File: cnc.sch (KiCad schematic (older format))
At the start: 9 parts, among them CON101 SD_Card, U101 pic32

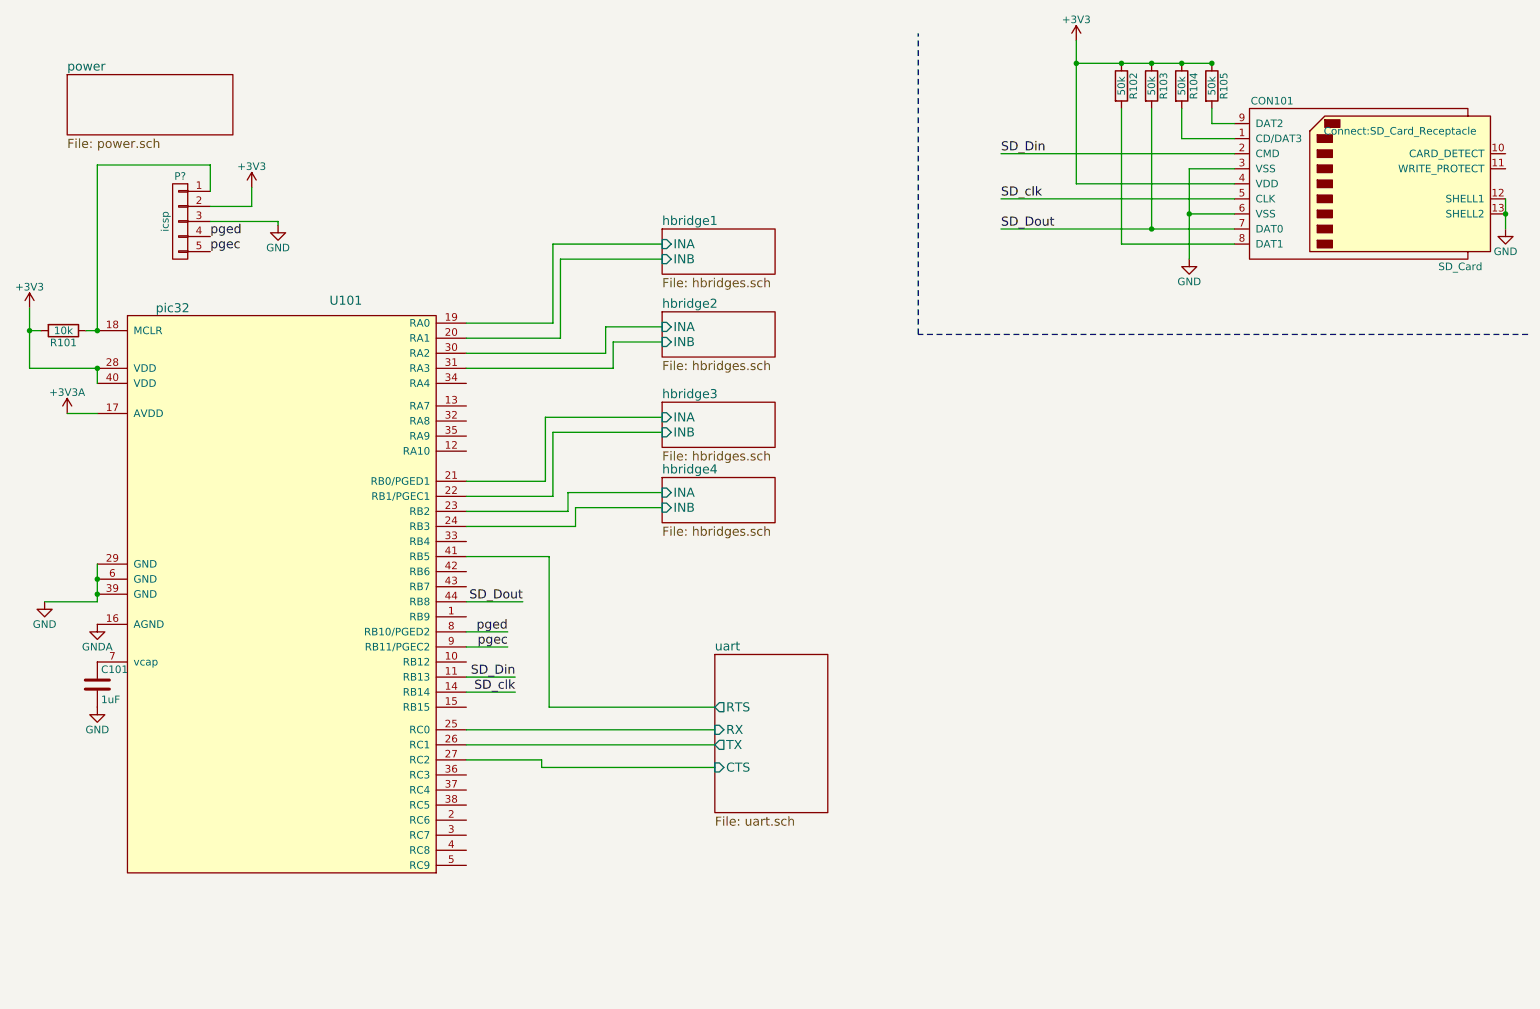
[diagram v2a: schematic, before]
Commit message: Routed a h-bridge. Damn that's a lot of work.
also assigned a lot of components.
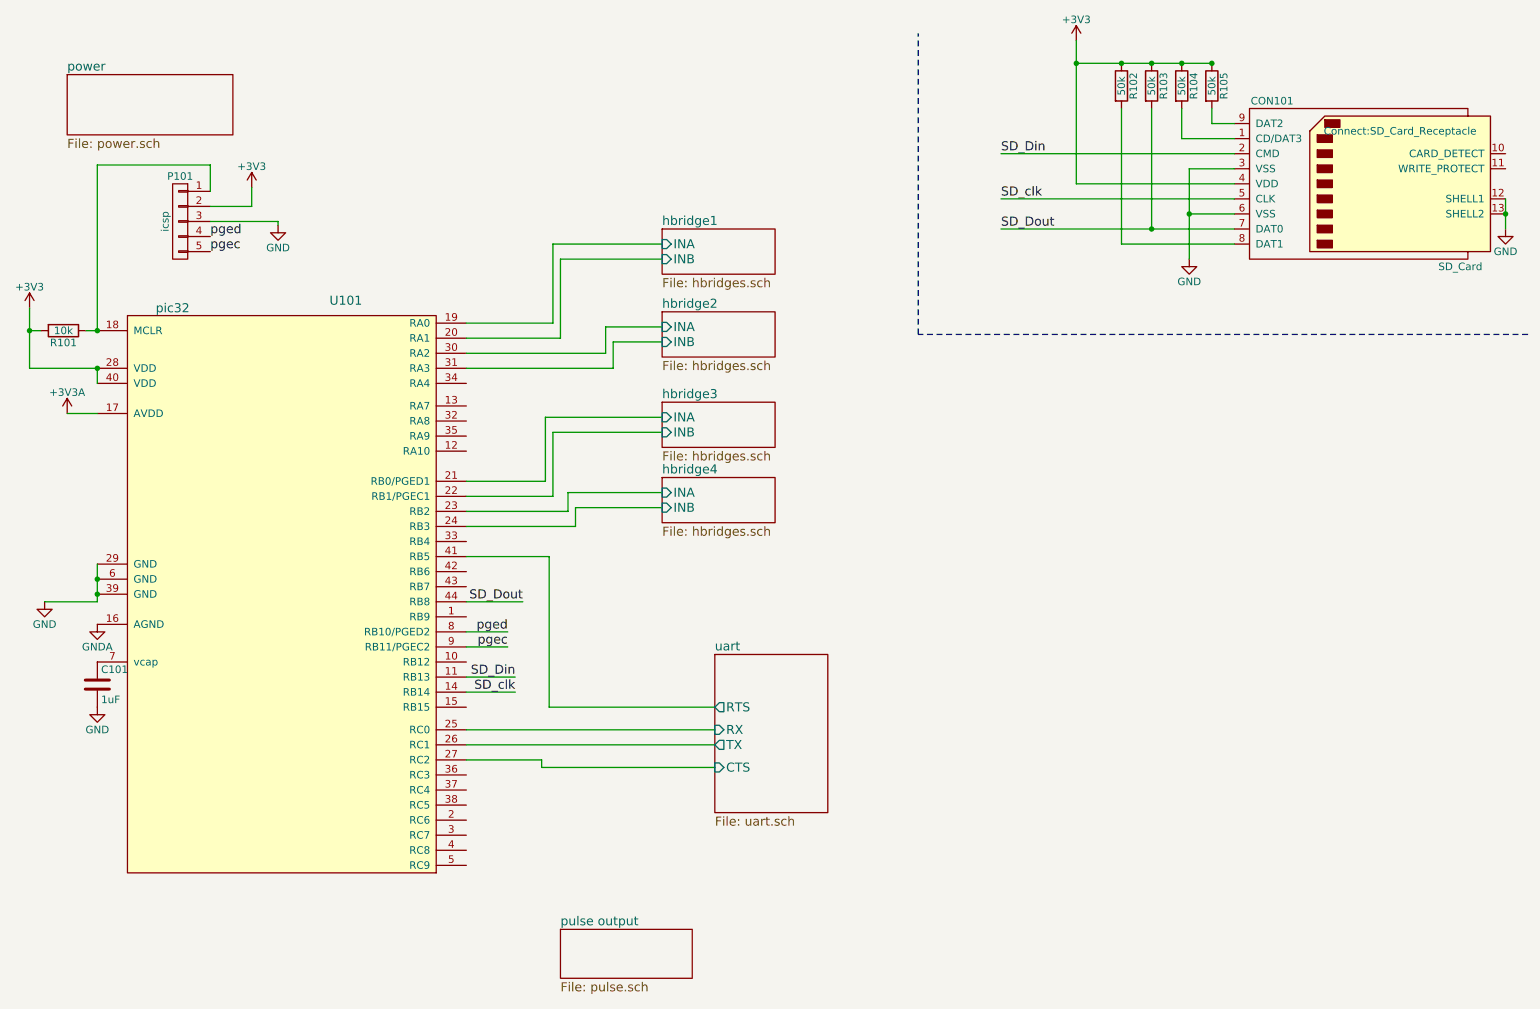
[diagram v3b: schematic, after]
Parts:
- P101: renamed from P?; footprint (none) -> Pin_Headers:Pin_Header_Straight_1x05
- R101, R102, R103, R104, R105: footprint Resistors_SMD:R_0805_HandSoldering -> lib:R_0402_handsoldering
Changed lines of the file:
@@
 $Descr A4 11693 8268
 encoding utf-8
-Sheet 1 7
+Sheet 1 8
 Title ""
 Date ""
@@
 F 0 "R101" V 1405 2675 50  0000 C CNN
 F 1 "10k" V 1325 2675 50  0000 C CNN
-F 2 "Resistors_SMD:R_0805_HandSoldering" V 1255 2675 50  0001 C CNN
+F 2 "lib:R_0402_handsoldering" V 1255 2675 50  0001 C CNN
 F 3 "" H 1325 2675 50  0000 C CNN
 	1    1325 2675
@@
 F 0 "R105" V 9030 1050 50  0000 C CNN
 F 1 "50k" V 8950 1050 50  0000 C CNN
-F 2 "Resistors_SMD:R_0805_HandSoldering" V 8880 1050 50  0001 C CNN
+F 2 "lib:R_0402_handsoldering" V 8880 1050 50  0001 C CNN
 F 3 "" H 8950 1050 50  0000 C CNN
 	1    8950 1050
@@
 F 0 "R104" V 8830 1050 50  0000 C CNN
 F 1 "50k" V 8750 1050 50  0000 C CNN
-F 2 "Resistors_SMD:R_0805_HandSoldering" V 8680 1050 50  0001 C CNN
+F 2 "lib:R_0402_handsoldering" V 8680 1050 50  0001 C CNN
 F 3 "" H 8750 1050 50  0000 C CNN
 	1    8750 1050
@@
 F 0 "R103" V 8630 1050 50  0000 C CNN
 F 1 "50k" V 8550 1050 50  0000 C CNN
-F 2 "Resistors_SMD:R_0805_HandSoldering" V 8480 1050 50  0001 C CNN
+F 2 "lib:R_0402_handsoldering" V 8480 1050 50  0001 C CNN
 F 3 "" H 8550 1050 50  0000 C CNN
 	1    8550 1050
@@
 F 0 "R102" V 8430 1050 50  0000 C CNN
 F 1 "50k" V 8350 1050 50  0000 C CNN
-F 2 "Resistors_SMD:R_0805_HandSoldering" V 8280 1050 50  0001 C CNN
+F 2 "lib:R_0402_handsoldering" V 8280 1050 50  0001 C CNN
 F 3 "" H 8350 1050 50  0000 C CNN
 	1    8350 1050
@@
 $EndSheet
 $Comp
-L CONN_01X05 P?
+L CONN_01X05 P101
 U 1 1 57BDB89F
 P 2100 1950
-F 0 "P?" H 2100 2250 50  0000 C CNN
+F 0 "P101" H 2100 2250 50  0000 C CNN
 F 1 "icsp" V 2200 1950 50  0000 C CNN
-F 2 "" H 2100 1950 50  0000 C CNN
+F 2 "Pin_Headers:Pin_Header_Straight_1x05" H 2100 1950 50  0001 C CNN
 F 3 "" H 2100 1950 50  0000 C CNN
 	1    2100 1950
@@
 	2300 1575 2300 1750
 $Comp
-L +3V3 #PWR?
+L +3V3 #PWR09
 U 1 1 57BDBEA3
 P 2575 1725
-F 0 "#PWR?" H 2575 1575 50  0001 C CNN
+F 0 "#PWR09" H 2575 1575 50  0001 C CNN
 F 1 "+3V3" H 2575 1865 50  0000 C CNN
 F 2 "" H 2575 1725 50  0000 C CNN
@@
 Connection ~ 1550 2925
 $Comp
-L GND #PWR?
+L GND #PWR010
 U 1 1 57BDC589
 P 2750 1975
-F 0 "#PWR?" H 2750 1725 50  0001 C CNN
+F 0 "#PWR010" H 2750 1725 50  0001 C CNN
 F 1 "GND" H 2750 1825 50  0000 C CNN
 F 2 "" H 2750 1975 50  0000 C CNN
@@
 Wire Wire Line
 	4000 4775 4275 4775
+$Sheet
+S 4625 6650 875  325
+U 57BDEEDC
+F0 "pulse output" 60
+F1 "pulse.sch" 60
+$EndSheet
 $EndSCHEMATC
